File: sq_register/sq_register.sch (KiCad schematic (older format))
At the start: 1 part, among them P1 DIN_41612_128P

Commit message: Page 2 of module 6, plus a few corrections.
Changed RPTSET in module 3 from an output to an input. Dropped unneeded
pullups from R1C/ (turns out this missing one is in module 6) and RB1/
(I don't remember why that was there) in module 4.
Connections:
- net 5XP4: now also P1.32 (32A); no longer P1.31 (31A)
- net ADS0: now also P1.49 (17B); no longer P1.48 (16B)
- net BR1B2B: now also P1.27 (27A); no longer P1.26 (26A)
- net BR2/: now also P1.26 (26A); no longer P1.25 (25A)
- net CCS0: now also P1.50 (18B); no longer P1.49 (17B)
- net CCS0/: now also P1.51 (19B); no longer P1.50 (18B)
- net DAS0: now also P1.52 (20B); no longer P1.51 (19B)
- net DAS0/: now also P1.53 (21B); no longer P1.52 (20B)
- net DAS1: now also P1.54 (22B); no longer P1.53 (21B)
- net DAS1/: now also P1.55 (23B); no longer P1.54 (22B)
- net DXCH0: now also P1.56 (24B); no longer P1.55 (23B)
- net EXST0/: now also P1.46 (14B); no longer P1.45 (13B)
- net EXST1/: now also P1.47 (15B); no longer P1.46 (14B)
- net EXT: now also P1.29 (29A); no longer P1.28 (28A)
- net EXTPLS: now also P1.30 (30A); no longer P1.29 (29A)
- net GND: no longer P1.98 (2D)
- net GOJ1: now also P1.57 (25B); no longer P1.56 (24B)
- net GOJ1/: now also P1.58 (26B); no longer P1.57 (25B)
- net IC1: now also P1.79 (15C); no longer P1.78 (14C)
- net IC10: now also P1.88 (24C); no longer P1.87 (23C)
- net IC10/: now also P1.89 (25C); no longer P1.88 (24C)
- net IC11/: now also P1.90 (26C); no longer P1.89 (25C)
- net IC12: now also P1.91 (27C); no longer P1.90 (26C)
- net IC12/: now also P1.92 (28C); no longer P1.91 (27C)
- net IC13: now also P1.93 (29C); no longer P1.92 (28C)
- net IC14: now also P1.94 (30C); no longer P1.93 (29C)
- net IC15: now also P1.95 (31C); no longer P1.94 (30C)
- net IC15/: now also P1.96 (32C); no longer P1.95 (31C)
- net IC16: now also P1.97 (1D); no longer P1.96 (32C)
- net IC16/: now also P1.98 (2D); no longer P1.97 (1D)
- net IC2: now also P1.80 (16C); no longer P1.79 (15C)
- net IC2/: now also P1.81 (17C); no longer P1.80 (16C)
- net IC3: now also P1.82 (18C); no longer P1.81 (17C)
- net IC4: now also P1.83 (19C); no longer P1.82 (18C)
- net IC5: now also P1.84 (20C); no longer P1.83 (19C)
- net IC5/: now also P1.85 (21C); no longer P1.84 (20C)
- net IC8/: now also P1.86 (22C); no longer P1.85 (21C)
- net IC9: now also P1.87 (23C); no longer P1.86 (22C)
- net KRPT: now also P1.21 (21A); no longer P1.20 (20A)
- net MASK0: now also P1.59 (27B); no longer P1.58 (26B)
- net MASK0/: now also P1.60 (28B); no longer P1.59 (27B)
- net MNHRPT: now also P1.34 (2B); no longer P1.33 (1B)
- net MP0: now also P1.61 (29B); no longer P1.60 (28B)
- net MP0/: now also P1.62 (30B); no longer P1.61 (29B)
- net MP1: now also P1.63 (31B); no longer P1.62 (30B)
- net MP3: now also P1.64 (32B); no longer P1.63 (31B)
- net MP3/: now also P1.65 (1C); no longer P1.64 (32B)
- net MP3A: now also P1.66 (2C); no longer P1.65 (1C)
- net MSU0: now also P1.67 (3C); no longer P1.66 (2C)
- net MSU0/: now also P1.68 (4C); no longer P1.67 (3C)
- net MTCSAI: now also P1.33 (1B); no longer P1.32 (32A)
- net NDX0/: now also P1.69 (5C); no longer P1.68 (4C)
- net NISQ: now also P1.31 (31A); no longer P1.30 (30A)
- net QC0/: now also P1.38 (6B); no longer P1.37 (5B)
- net QC1/: now also P1.39 (7B); no longer P1.38 (6B)
- net QC2/: now also P1.40 (8B); no longer P1.39 (7B)
- net QC3/: now also P1.41 (9B); no longer P1.40 (8B)
- net QXCH0/: now also P1.70 (6C); no longer P1.69 (5C)
- net RSM3: now also P1.71 (7C); no longer P1.70 (6C)
- net RSM3/: now also P1.72 (8C); no longer P1.71 (7C)
- net RXOR0: now also P1.28 (28A); no longer P1.27 (27A)
- net SQ0/: now also P1.35 (3B); no longer P1.34 (2B)
- net SQ1/: now also P1.36 (4B); no longer P1.35 (3B)
- net SQ2/: now also P1.37 (5B); no longer P1.36 (4B)
- net SQEXT/: now also P1.45 (13B); no longer P1.44 (12B)
- net SQR10: now also P1.43 (11B); no longer P1.42 (10B)
- net SQR10/: now also P1.44 (12B); no longer P1.43 (11B)
- net SQR12/: now also P1.42 (10B); no longer P1.41 (9B)
- net ST0/: now also P1.22 (22A); no longer P1.21 (21A)
- net ST1/: now also P1.23 (23A); no longer P1.22 (22A)
- net ST3/: now also P1.25 (25A); no longer P1.24 (24A)
- net STD2: now also P1.24 (24A); no longer P1.23 (23A)
- net STRTFC: now also P1.48 (16B); no longer P1.47 (15B)
- net TC0: now also P1.73 (9C); no longer P1.72 (8C)
- net TC0/: now also P1.74 (10C); no longer P1.73 (9C)
- net TCF0: now also P1.75 (11C); no longer P1.74 (10C)
- net TCSAJ3/: now also P1.76 (12C); no longer P1.75 (11C)
- net TS0: now also P1.77 (13C); no longer P1.76 (12C)
- net TS0/: now also P1.78 (14C); no longer P1.77 (13C)
- new net RPTSET: P1.20 (20A)
- no-connect marks 53 -> 52

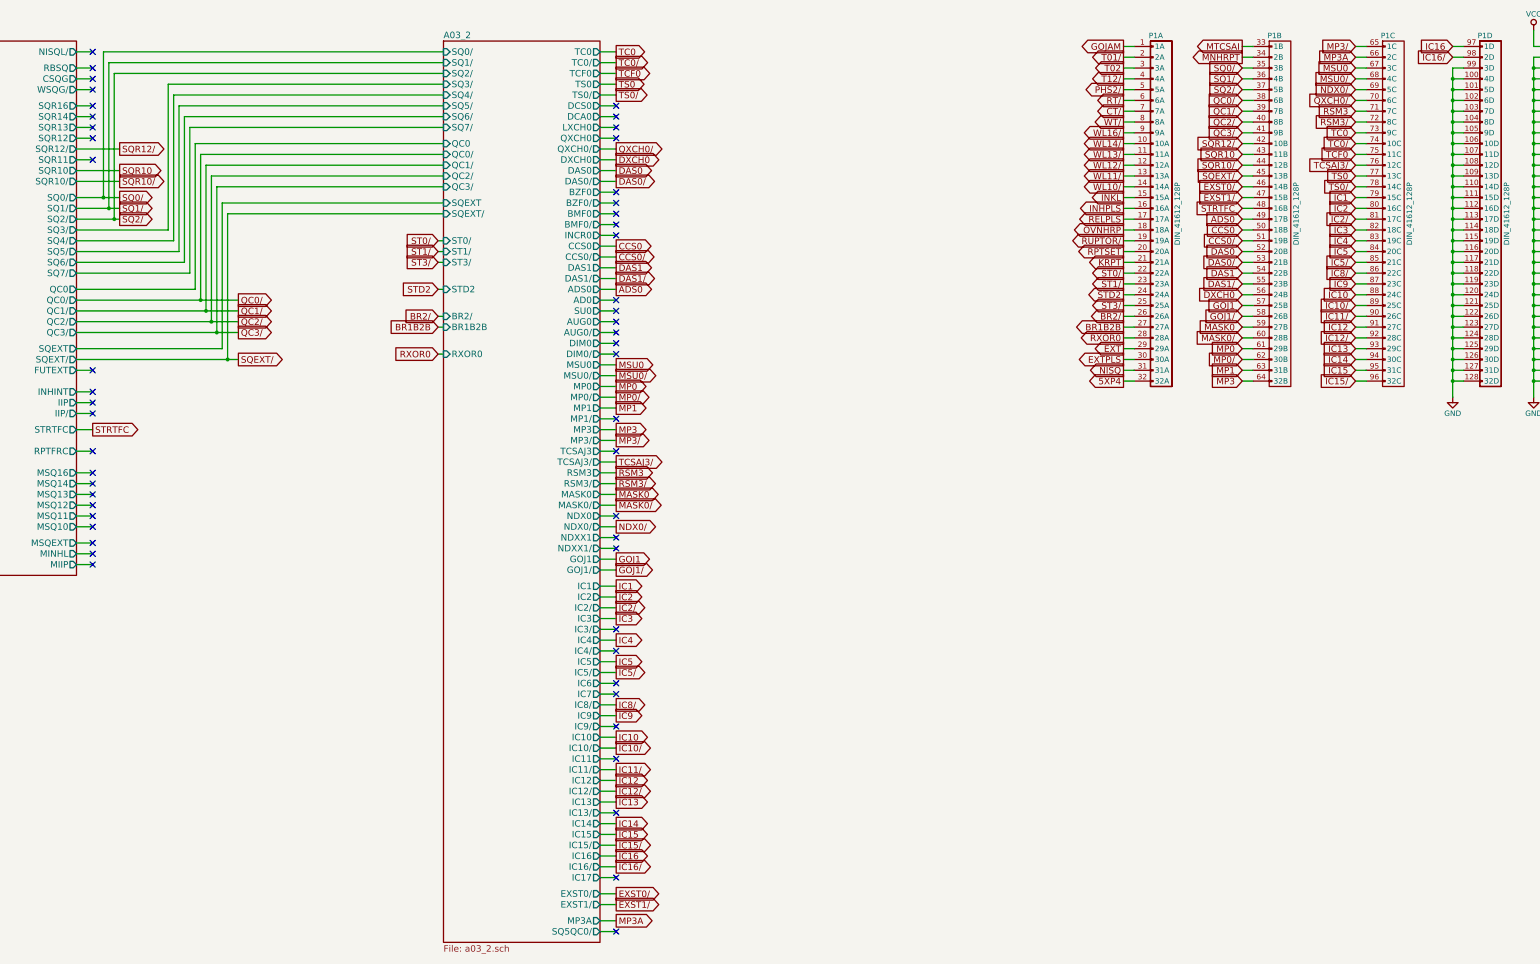
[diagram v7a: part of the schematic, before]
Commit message: Tied in module 6 and corrected a handful of naming/routing errors... most notably some missing gates from A06-1
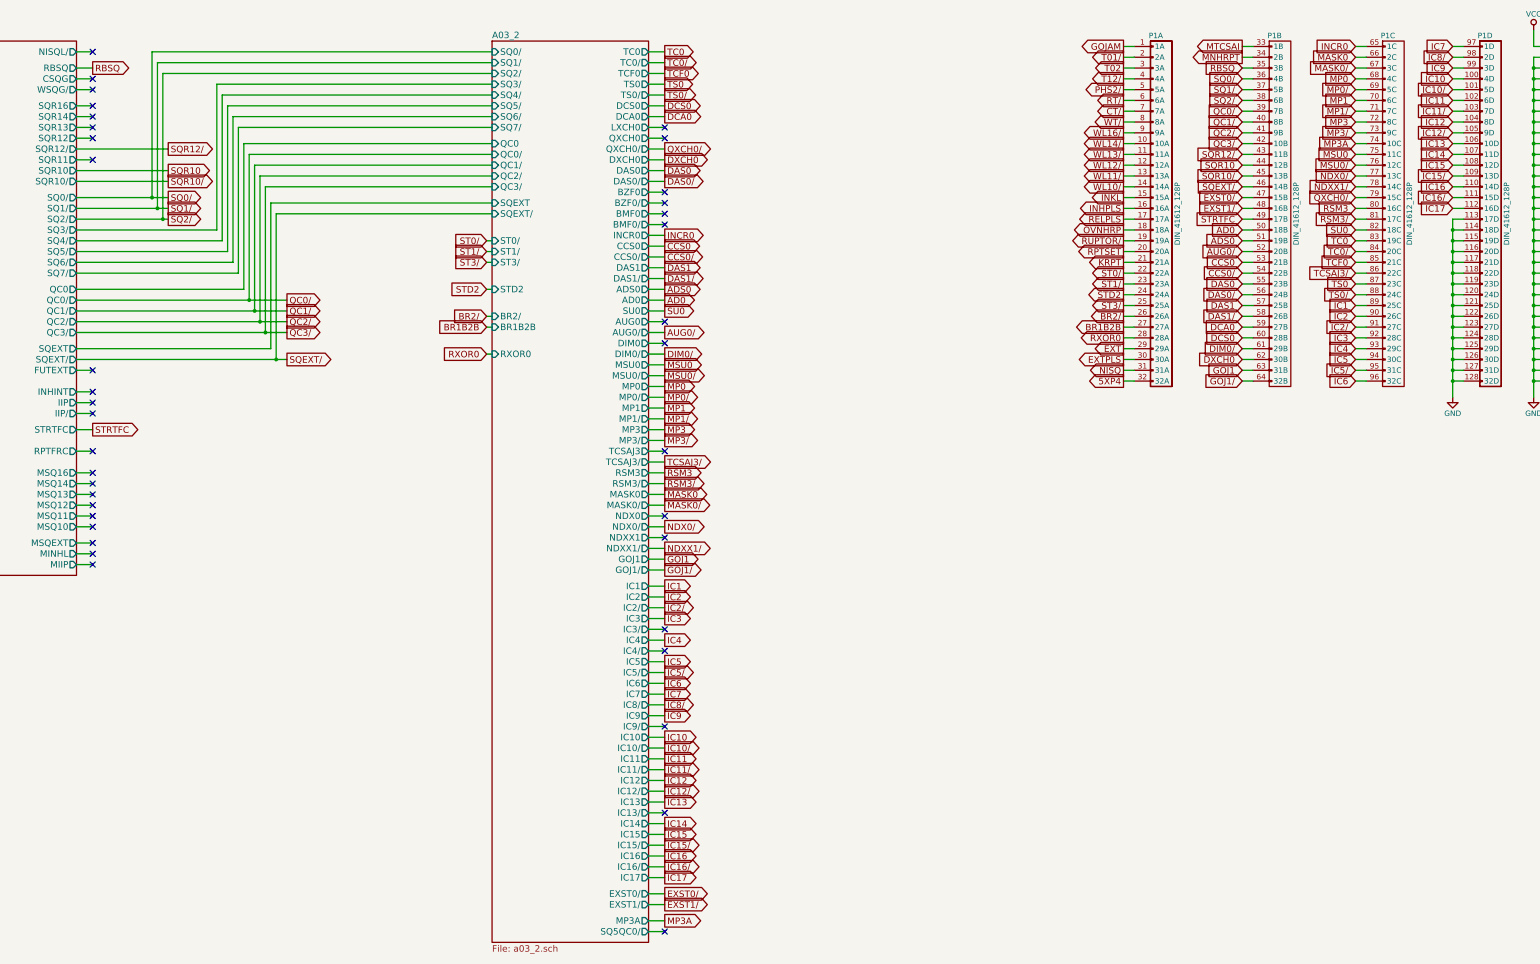
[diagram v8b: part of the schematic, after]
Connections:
- net ADS0: now also P1.51 (19B); no longer P1.49 (17B)
- net CCS0: now also P1.53 (21B); no longer P1.50 (18B)
- net CCS0/: now also P1.54 (22B); no longer P1.51 (19B)
- net DAS0: now also P1.55 (23B); no longer P1.52 (20B)
- net DAS0/: now also P1.56 (24B); no longer P1.53 (21B)
- net DAS1: now also P1.57 (25B); no longer P1.54 (22B)
- net DAS1/: now also P1.58 (26B); no longer P1.55 (23B)
- net DXCH0: now also P1.62 (30B); no longer P1.56 (24B)
- net EXST0/: now also P1.47 (15B); no longer P1.46 (14B)
- net EXST1/: now also P1.48 (16B); no longer P1.47 (15B)
- net GND: no longer P1.100 (4D), P1.101 (5D), P1.102 (6D), P1.103 (7D), P1.104 (8D), P1.105 (9D), P1.106 (10D), P1.107 (11D), P1.108 (12D), P1.109 (13D), P1.110 (14D), P1.111 (15D), P1.112 (16D), P1.99 (3D)
- net GOJ1: now also P1.63 (31B); no longer P1.57 (25B)
- net GOJ1/: now also P1.64 (32B); no longer P1.58 (26B)
- net IC1: now also P1.89 (25C); no longer P1.79 (15C)
- net IC10: now also P1.100 (4D); no longer P1.88 (24C)
- net IC10/: now also P1.101 (5D); no longer P1.89 (25C)
- net IC11/: now also P1.103 (7D); no longer P1.90 (26C)
- net IC12: now also P1.104 (8D); no longer P1.91 (27C)
- net IC12/: now also P1.105 (9D); no longer P1.92 (28C)
- net IC13: now also P1.106 (10D); no longer P1.93 (29C)
- net IC14: now also P1.107 (11D); no longer P1.94 (30C)
- net IC15: now also P1.108 (12D); no longer P1.95 (31C)
- net IC15/: now also P1.109 (13D); no longer P1.96 (32C)
- net IC16: now also P1.110 (14D); no longer P1.97 (1D)
- net IC16/: now also P1.111 (15D); no longer P1.98 (2D)
- net IC2: now also P1.90 (26C); no longer P1.80 (16C)
- net IC2/: now also P1.91 (27C); no longer P1.81 (17C)
- net IC3: now also P1.92 (28C); no longer P1.82 (18C)
- net IC4: now also P1.93 (29C); no longer P1.83 (19C)
- net IC5: now also P1.94 (30C); no longer P1.84 (20C)
- net IC5/: now also P1.95 (31C); no longer P1.85 (21C)
- net IC8/: now also P1.98 (2D); no longer P1.86 (22C)
- net IC9: now also P1.99 (3D); no longer P1.87 (23C)
- net MASK0: now also P1.66 (2C); no longer P1.59 (27B)
- net MASK0/: now also P1.67 (3C); no longer P1.60 (28B)
- net MP0: now also P1.68 (4C); no longer P1.61 (29B)
- net MP0/: now also P1.69 (5C); no longer P1.62 (30B)
- net MP1: now also P1.70 (6C); no longer P1.63 (31B)
- net MP3: now also P1.72 (8C); no longer P1.64 (32B)
- net MP3/: now also P1.73 (9C); no longer P1.65 (1C)
- net MP3A: now also P1.74 (10C); no longer P1.66 (2C)
- net MSU0: now also P1.75 (11C); no longer P1.67 (3C)
- net MSU0/: now also P1.76 (12C); no longer P1.68 (4C)
- net NDX0/: now also P1.77 (13C); no longer P1.69 (5C)
- net QC0/: now also P1.39 (7B); no longer P1.38 (6B)
- net QC1/: now also P1.40 (8B); no longer P1.39 (7B)
- net QC2/: now also P1.41 (9B); no longer P1.40 (8B)
- net QC3/: now also P1.42 (10B); no longer P1.41 (9B)
- net QXCH0/: now also P1.79 (15C); no longer P1.70 (6C)
- net RSM3: now also P1.80 (16C); no longer P1.71 (7C)
- net RSM3/: now also P1.81 (17C); no longer P1.72 (8C)
- net SQ0/: now also P1.36 (4B); no longer P1.35 (3B)
- net SQ1/: now also P1.37 (5B); no longer P1.36 (4B)
- net SQ2/: now also P1.38 (6B); no longer P1.37 (5B)
- net SQEXT/: now also P1.46 (14B); no longer P1.45 (13B)
- net SQR10: now also P1.44 (12B); no longer P1.43 (11B)
- net SQR10/: now also P1.45 (13B); no longer P1.44 (12B)
- net SQR12/: now also P1.43 (11B); no longer P1.42 (10B)
- net STRTFC: now also P1.49 (17B); no longer P1.48 (16B)
- net TC0: now also P1.83 (19C); no longer P1.73 (9C)
- net TC0/: now also P1.84 (20C); no longer P1.74 (10C)
- net TCF0: now also P1.85 (21C); no longer P1.75 (11C)
- net TCSAJ3/: now also P1.86 (22C); no longer P1.76 (12C)
- net TS0: now also P1.87 (23C); no longer P1.77 (13C)
- net TS0/: now also P1.88 (24C); no longer P1.78 (14C)
- new net AD0: P1.50 (18B)
- new net AUG0/: P1.52 (20B)
- new net DCA0: P1.59 (27B)
- new net DCS0: P1.60 (28B)
- new net DIM0/: P1.61 (29B)
- new net IC11: P1.102 (6D)
- new net IC17: P1.112 (16D)
- new net IC6: P1.96 (32C)
- new net IC7: P1.97 (1D)
- new net INCR0: P1.65 (1C)
- new net MP1/: P1.71 (7C)
- new net NDXX1/: P1.78 (14C)
- new net RBSQ: P1.35 (3B)
- new net SU0: P1.82 (18C)
- no-connect marks 52 -> 38
